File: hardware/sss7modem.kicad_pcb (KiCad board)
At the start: 2 copper layers, 34.4 x 34.3 mm, 18 parts, among them IC1 MCP2551-I/SN, K1 CONN_3, P1 CONN_4

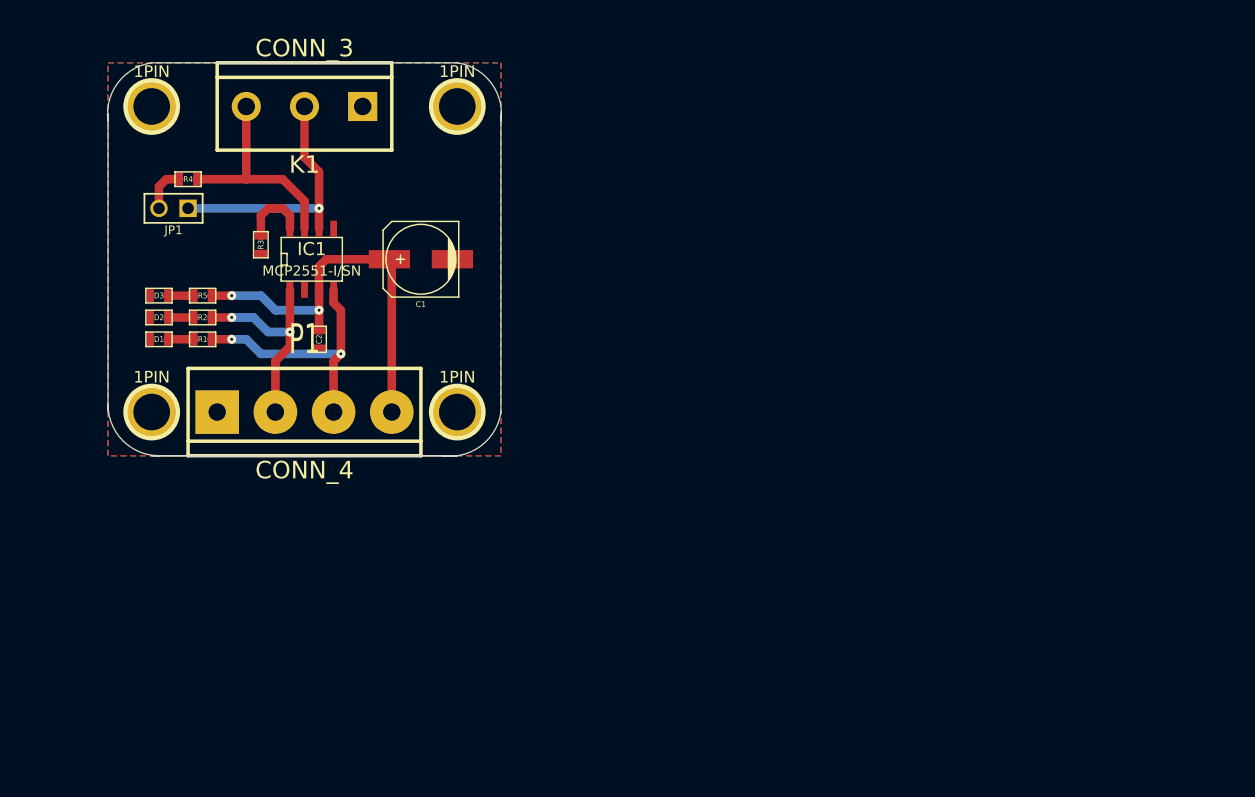
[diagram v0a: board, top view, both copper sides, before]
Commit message: Changed schematic for floating common on bus side
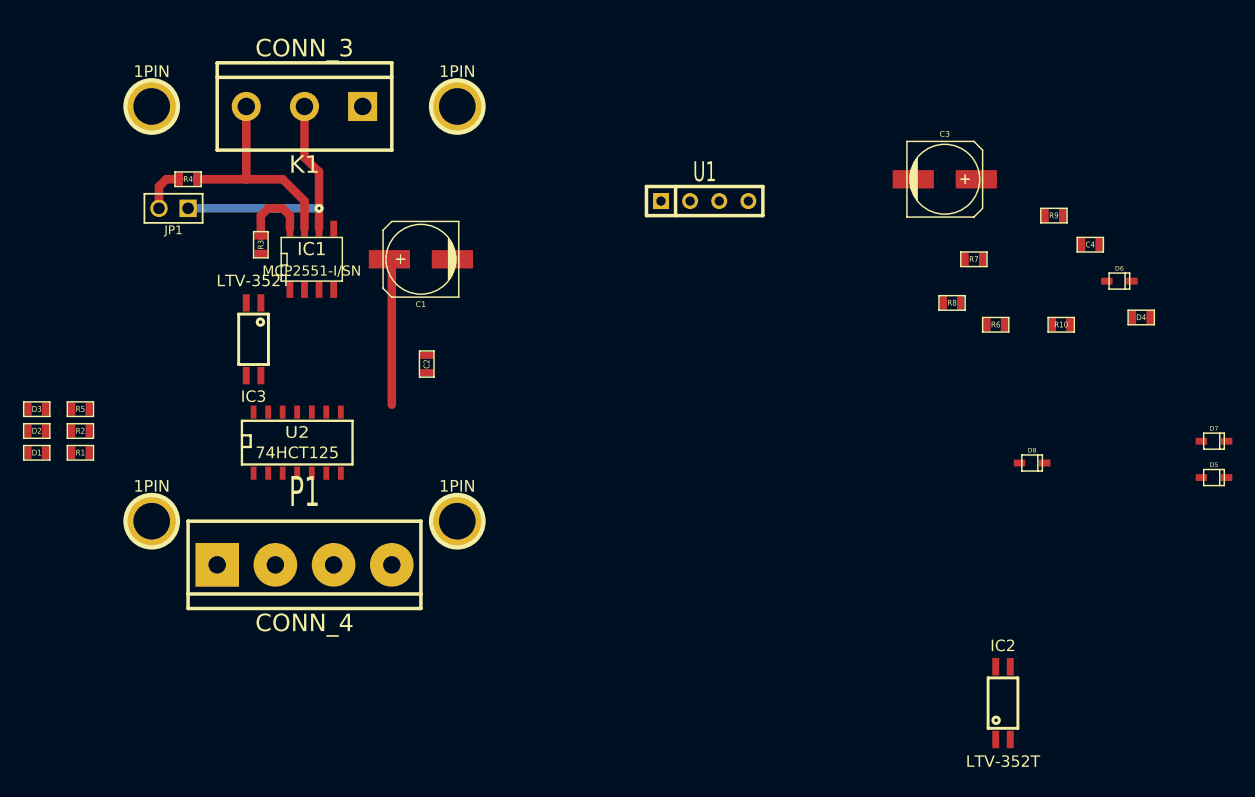
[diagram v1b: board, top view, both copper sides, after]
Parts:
- added C3: 47uF, c_elec_6.3x5.8, F.Cu at (96.5, 36.2)
- added C4: 100nF, SM0603, F.Cu at (109.2, 41.9)
- added D4: LED, SM0603, F.Cu at (113.7, 48.3)
- added D5: DIODE, sod323, F.Cu at (120.0, 62.2)
- added D6: DIODE, sod323, F.Cu at (111.8, 45.1)
- added D7: DIODE, sod323, F.Cu at (120.0, 59.1)
- added D8: DIODE, sod323, F.Cu at (104.1, 61.0)
- added IC2: LTV-352T, mfp_4, F.Cu at (101.6, 81.9)
- added IC3: LTV-352T, mfp_4, F.Cu at (36.2, 50.2)
- added R10: 1k, SM0603, F.Cu at (106.7, 48.9)
- added R6: 390, SM0603, F.Cu at (101.0, 48.9)
- added R7: R, SM0603, F.Cu at (99.1, 43.2)
- added R8: 390, SM0603, F.Cu at (97.2, 47.0)
- added R9: 1k, SM0603, F.Cu at (106.0, 39.4)
- added U1: SIM1-0505, SIL-4, F.Cu at (75.6, 38.1)
- added U2: 74HCT125, SO14E, F.Cu at (40.0, 59.1)
- moved D3 14.6 mm to (17.3, 56.3)
- moved R5 14.6 mm to (21.1, 56.3)
- moved D1 14.6 mm to (17.3, 60.1)
- moved D2 14.6 mm to (17.3, 58.2)
- moved R1 14.6 mm to (21.1, 60.1)
- moved R2 14.6 mm to (21.1, 58.2)
- moved P1 13.3 mm to (40.6, 69.8)
- moved C2 9.64 mm to (51.3, 52.3)
- moved 1PIN 9.53 mm to (54.0, 66.0)
- moved 1PIN 9.53 mm to (27.3, 66.0)
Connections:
- D1 pad 1: GND -> N-000006
- D1 pad 2: N-000009 -> TXD
- D2 pad 1: GND -> N-000005
- D2 pad 2: N-0000010 -> RXD
- IC1 pad 1: N-0000012 -> N-0000021
- IC1 pad 2: GND -> BUS_GND
- IC1 pad 3: +5V -> BUS_5V
- IC1 pad 4: N-0000011 -> N-0000022
- K1 pad 1: GND -> BUS_GND
- P1 pad 2: N-0000012 -> RXDout
- P1 pad 3: N-0000011 -> TXDin
- R1 pad 1: N-0000011 -> +5V
- R1 pad 2: N-000009 -> N-000006
- R2 pad 1: N-0000012 -> +5V
- R2 pad 2: N-0000010 -> N-000005
- R3 pad 2: GND -> BUS_GND
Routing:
- net N-0000011: track 22.4 -> 0.00 mm, vias 2 -> 0
- net +5V: track 34.7 -> 12.8 mm, vias 2 -> 0
- net N-0000012: track 17.9 -> 0.00 mm, vias 2 -> 0
- net N-000009: track 2.29 -> 0.00 mm
- net N-0000020: track 2.29 -> 0.00 mm
- net N-0000010: track 2.29 -> 0.00 mm
- removed copper zone on B.Cu, net GND
- removed copper zone on F.Cu, net GND
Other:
- board outline removed

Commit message: First draft for the split ground pcb
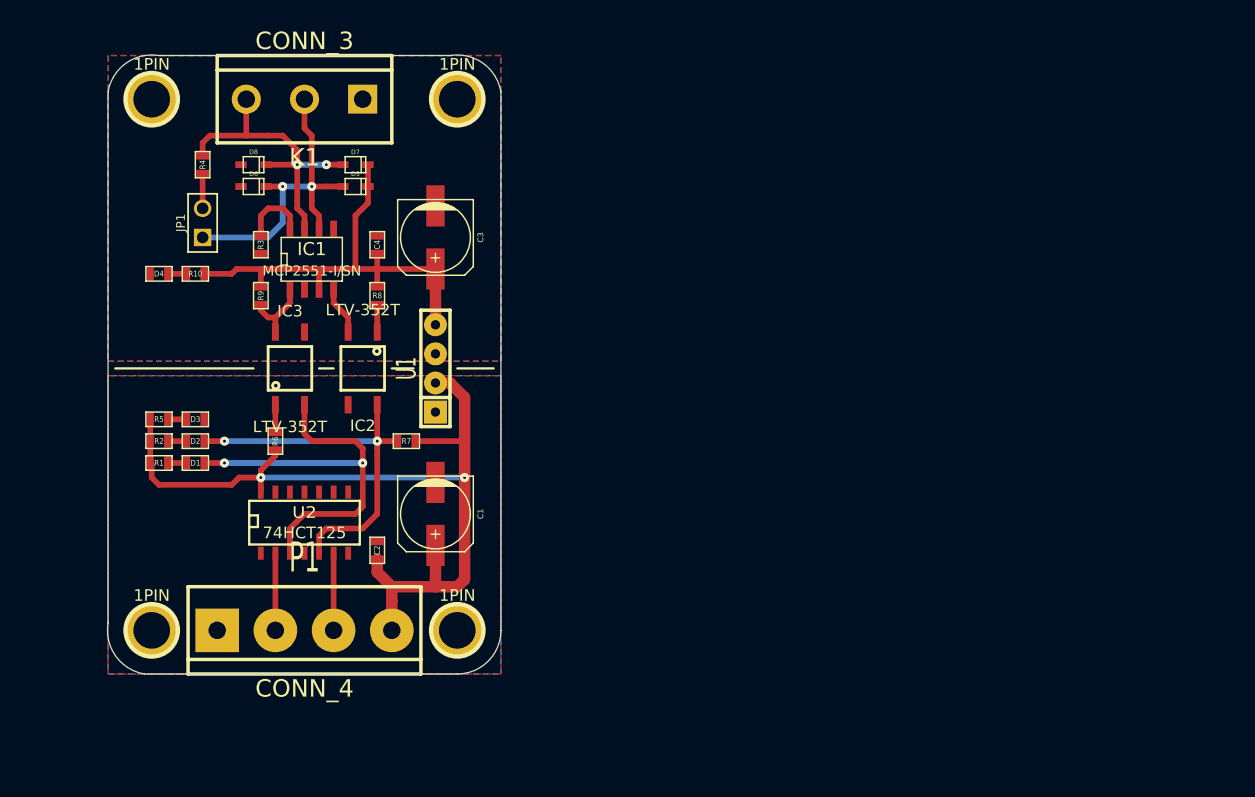
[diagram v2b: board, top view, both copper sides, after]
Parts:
- IC2, IC3: footprint mfp_4 -> mfsop6
- moved D4 85.8 mm to (27.9, 44.5), turned to 180 degrees
- moved D5 79.1 mm to (45.1, 36.8)
- moved D7 78.7 mm to (45.1, 34.9)
- moved D6 76.0 mm to (36.2, 36.8)
- moved R10 75.7 mm to (31.1, 44.5), turned to 180 degrees
- moved D8 72.8 mm to (36.2, 34.9)
- moved R9 69.6 mm to (36.8, 46.4), turned to 270 degrees
- moved R6 63.7 mm to (38.1, 59.1), turned to 90 degrees
- moved IC2 63.1 mm to (45.7, 52.7), turned to 180 degrees
- moved C4 62.2 mm to (47.0, 41.9), turned to 90 degrees
- moved R7 52.0 mm to (49.5, 59.1), turned to 180 degrees
- moved R8 50.2 mm to (47.0, 46.4), turned to 270 degrees
- moved C3 44.7 mm to (52.1, 41.3), turned to 270 degrees
- moved U1 27.7 mm to (52.1, 52.7), turned to 90 degrees
- moved C1 22.3 mm to (52.1, 65.4), turned to 270 degrees
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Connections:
- P1 pad 2: RXDout -> TXDin
- P1 pad 3: TXDin -> RXDout
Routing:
- net +5V: track 12.8 -> 77.4 mm, vias 0 -> 2
- net BUS_5V: track 0.00 -> 41.7 mm
- net TXD: track 0.00 -> 36.4 mm, vias 0 -> 2
- net RXD: track 0.00 -> 33.8 mm, vias 0 -> 2
- net N-0000025: track 19.0 -> 27.3 mm, vias 0 -> 2
- net N-0000026: track 22.6 -> 29.4 mm
- net TXDin: track 0.00 -> 6.73 mm
- net RXDout: track 0.00 -> 6.73 mm
- net N-0000021: track 0.00 -> 6.25 mm
- net N-0000022: track 0.00 -> 4.21 mm
- net N-0000023: track 0.00 -> 2.41 mm
- net N-000004: track 0.00 -> 2.41 mm
- net N-000007: track 0.00 -> 1.65 mm
- net N-000006: track 0.00 -> 1.65 mm
- net N-000005: track 0.00 -> 1.65 mm
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- added copper zone on B.Cu, net BUS_GND
- added copper zone on F.Cu, net BUS_GND
- added copper zone on B.Cu, net GND
- added copper zone on F.Cu, net GND
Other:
- board outline added: 34.3 x 54 mm

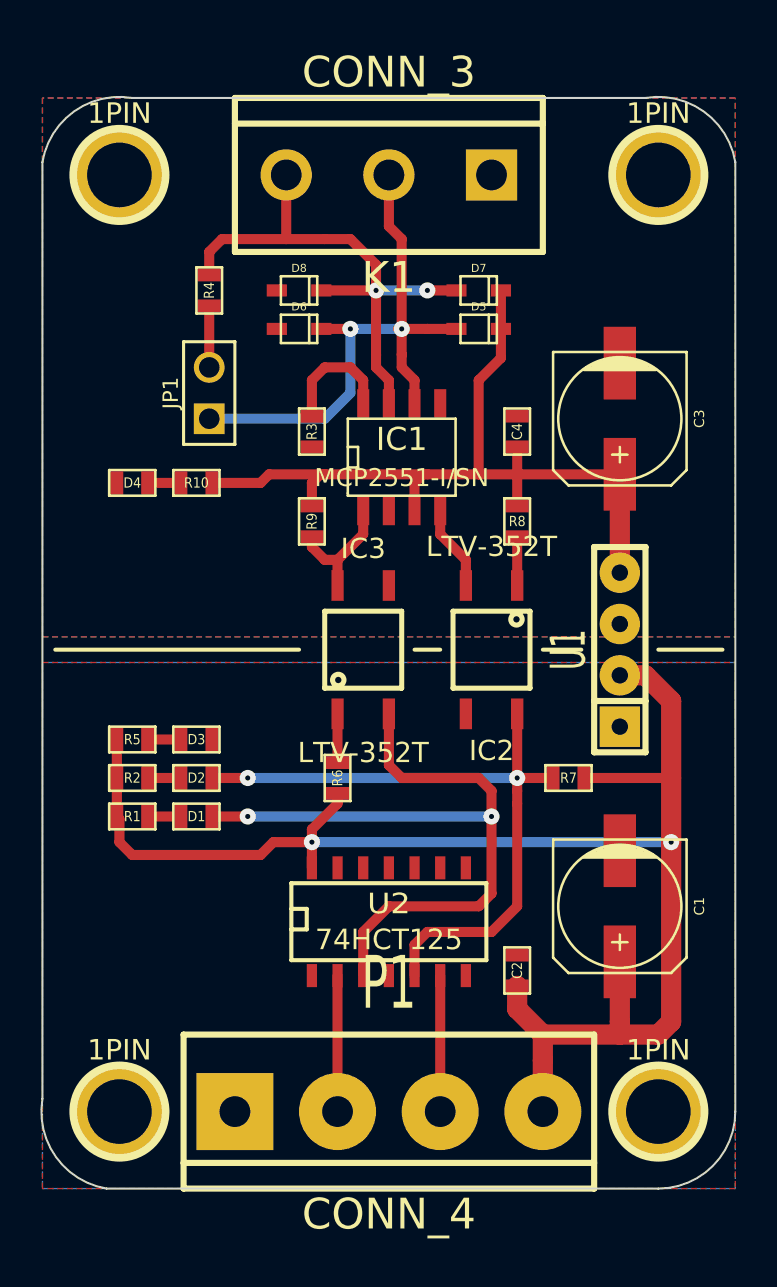
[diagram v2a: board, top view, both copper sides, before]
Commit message: Made boards smaller for panalizing
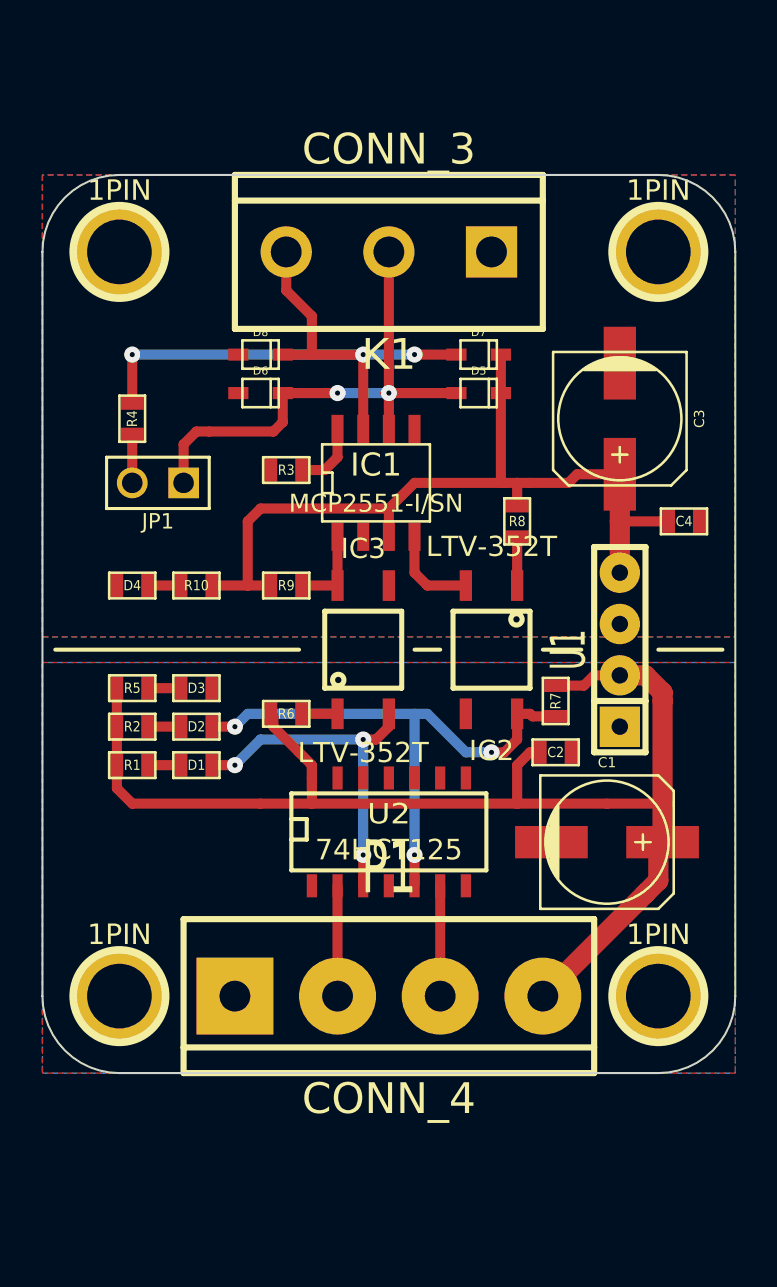
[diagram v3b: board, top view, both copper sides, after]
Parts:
- moved C2 11.0 mm to (48.9, 57.8), turned to 0 degrees
- moved C4 9.38 mm to (55.2, 46.4), turned to 0 degrees
- moved R4 7.41 mm to (27.9, 41.3)
- moved 1PIN 5.72 mm to (54.0, 69.8)
- moved 1PIN 5.72 mm to (27.3, 69.8)
- moved P1 5.72 mm to (40.6, 69.8)
- moved JP1 5.12 mm to (29.2, 44.5), turned to 180 degrees
- moved D4 5.08 mm to (27.9, 49.5)
- moved R10 5.08 mm to (31.1, 49.5)
- moved U2 4.45 mm to (40.6, 61.6)
- moved R6 4.07 mm to (35.6, 55.9), turned to 0 degrees
- moved R7 3.86 mm to (48.9, 55.2), turned to 270 degrees
- moved 1PIN 3.81 mm to (54.0, 33.0)
- moved 1PIN 3.81 mm to (27.3, 33.0)
- moved K1 3.81 mm to (40.6, 33.0)
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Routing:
- net TXD: track 36.4 -> 17.4 mm, vias 2 -> 3
- net +5V: track 77.4 -> 64.6 mm, vias 2 -> 0
- net RXD: track 33.8 -> 28.2 mm, vias 2 -> 3
- net N-0000025: track 27.3 -> 31.9 mm, vias 2 -> 3
- net N-0000026: track 29.4 -> 26.2 mm
- net N-0000027: track 5.99 -> 3.44 mm
- net N-0000021: track 6.25 -> 4.19 mm
- net N-000004: track 2.41 -> 1.78 mm
- net N-0000024: track 3.05 -> 2.41 mm
- net TXDin: track 6.73 -> 6.10 mm
- net RXDout: track 6.73 -> 6.10 mm
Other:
- board size 34.3 x 54 mm -> 34.3 x 44.4 mm

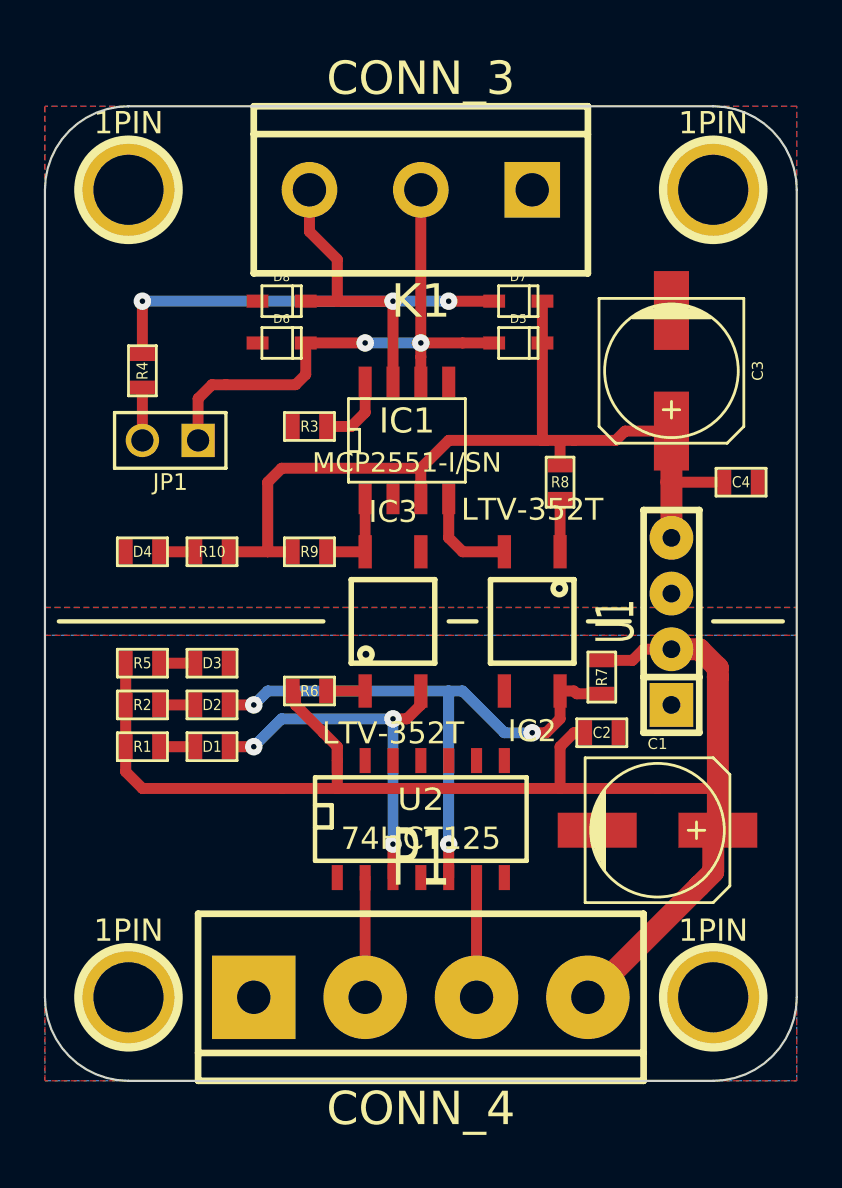
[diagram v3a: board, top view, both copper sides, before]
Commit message: Added logos, started to clean up silkscreen
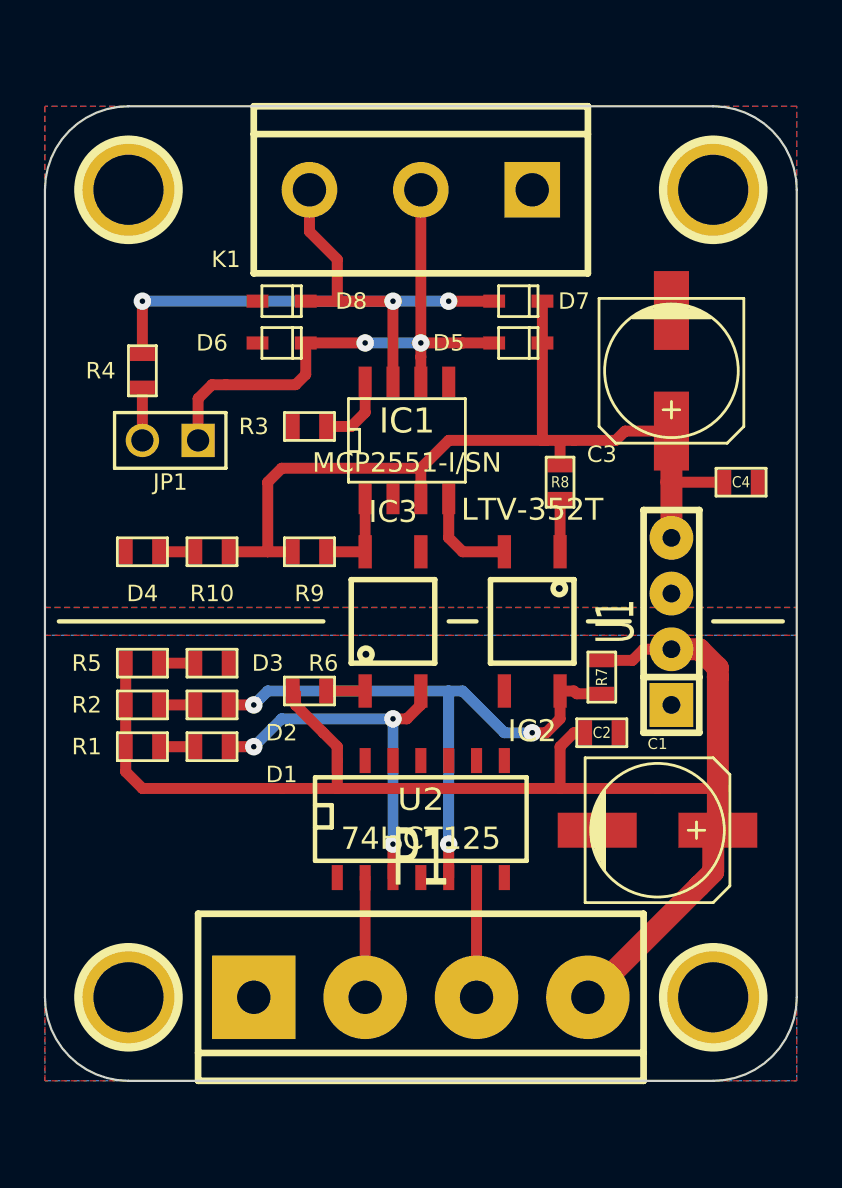
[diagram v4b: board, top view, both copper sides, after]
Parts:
- added G***: seidenstrasse_silkbot_15_00mm, seidenstrasse_silkbot_15_00mm, B.Cu at (40.6, 42.5)
- added G***: chaosinkl_silkbot_15_00mm, chaosinkl_silkbot_15_00mm, B.Cu at (48.9, 61.0)
- added G***: logo_hacker_silkbot_10_00mm, logo_hacker_silkbot_10_00mm, B.Cu at (30.5, 59.7)
